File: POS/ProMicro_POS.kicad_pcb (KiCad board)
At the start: 2 copper layers, 17.8 x 30.5 mm, 36 parts, among them J1 uFL, J2 Coax, U1 MPU-9250, U2 AP2112K-1.8, U3 SIM28ML

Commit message: clean
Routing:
- net SDA: track 13.8 -> 14.4 mm
- net GND: vias 49 -> 48

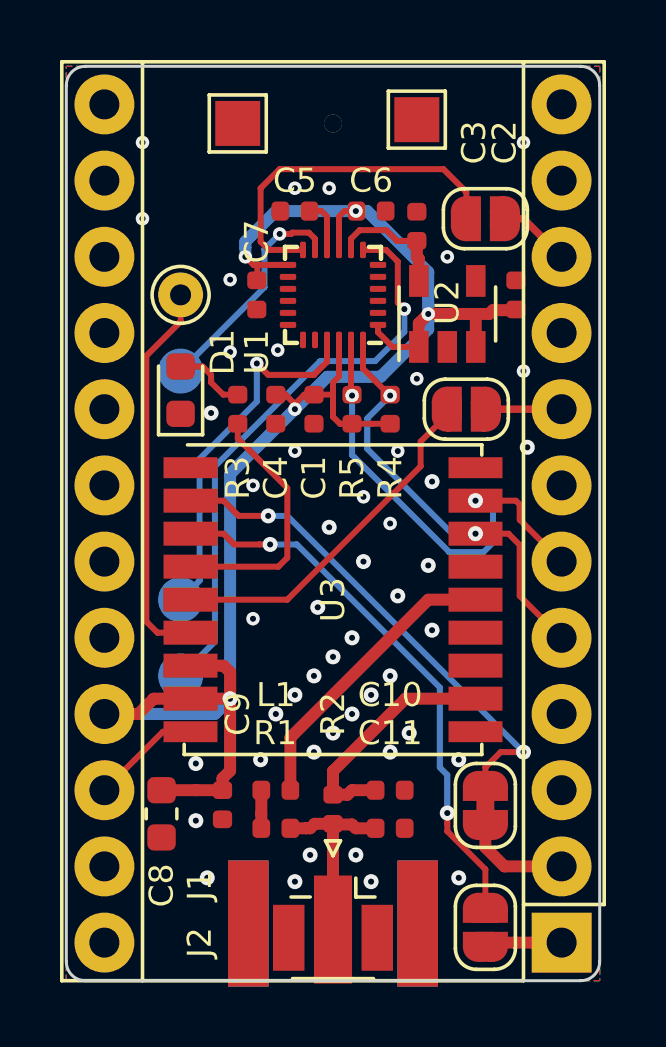
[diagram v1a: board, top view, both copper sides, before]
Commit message: fix ERC/DRC and add power planes
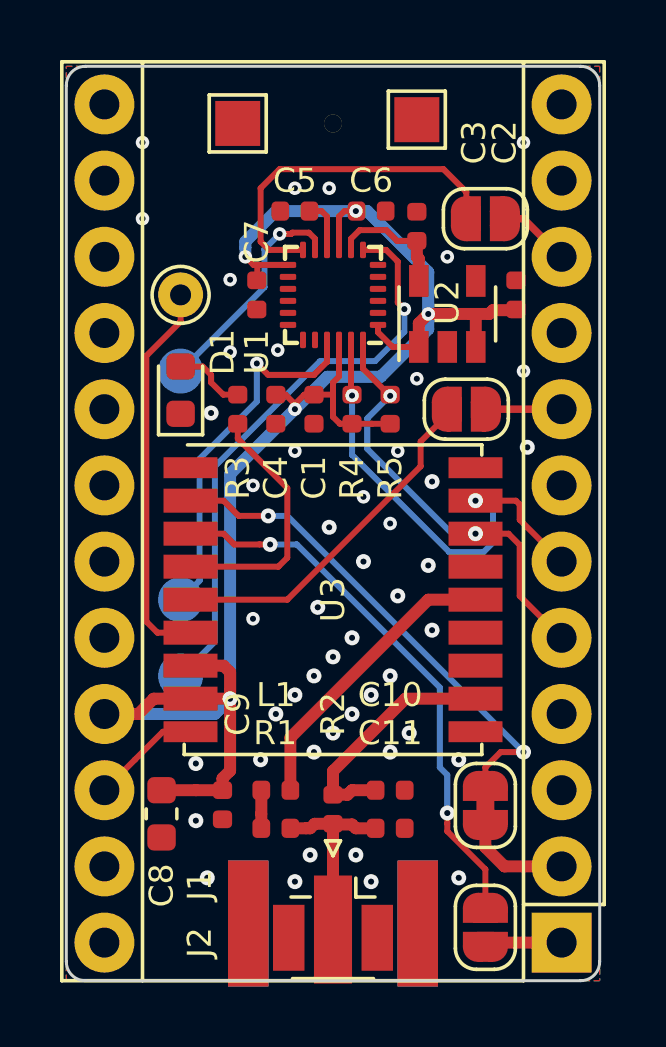
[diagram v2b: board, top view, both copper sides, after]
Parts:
- moved R4 1.27 mm to (145.4, 83.8)
- moved R5 1.27 mm to (146.7, 83.8)
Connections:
- A1 pad 10: (no net) -> INT
- A1 pad 11: (no net) -> Net-(A1-Pad11)
- A1 pad 12: (no net) -> Net-(A1-Pad12)
- A1 pad 13: (no net) -> Net-(A1-Pad13)
- A1 pad 14: (no net) -> Net-(A1-Pad14)
- A1 pad 15: (no net) -> Net-(A1-Pad15)
- A1 pad 16: (no net) -> Net-(A1-Pad16)
- A1 pad 17: (no net) -> Net-(A1-Pad17)
- A1 pad 18: (no net) -> Net-(A1-Pad18)
- A1 pad 19: (no net) -> Net-(A1-Pad19)
- A1 pad 20: (no net) -> Net-(A1-Pad20)
- A1 pad 24: (no net) -> +5V
- A1 pad 7: (no net) -> Net-(A1-Pad7)
- A1 pad 9: (no net) -> Net-(A1-Pad9)
- JP1 pad 2: (no net) -> INT
- R4 pad 2: SDA -> SCL
- R5 pad 2: SCL -> SDA
- U2 pad 4: (no net) -> Net-(U2-Pad4)
- U3 pad 13: (no net) -> Net-(U3-Pad13)
- U3 pad 15: (no net) -> Net-(U3-Pad15)
- U3 pad 18: (no net) -> Net-(U3-Pad18)
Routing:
- net INT: track 0.00 -> 2.43 mm
- net (no net): track 2.43 -> 0.00 mm
- added copper zone on In2.Cu, net +3V3
- added copper zone on In1.Cu, net GND
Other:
- copper layers 2 -> 4
- board text added: "nerdyscout.github.io/ ProMicro/POS v3.3"
- board text removed: "nerdyscout.github.io/ ProMicro/POS v3.1"

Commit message: make controller holes wide enough
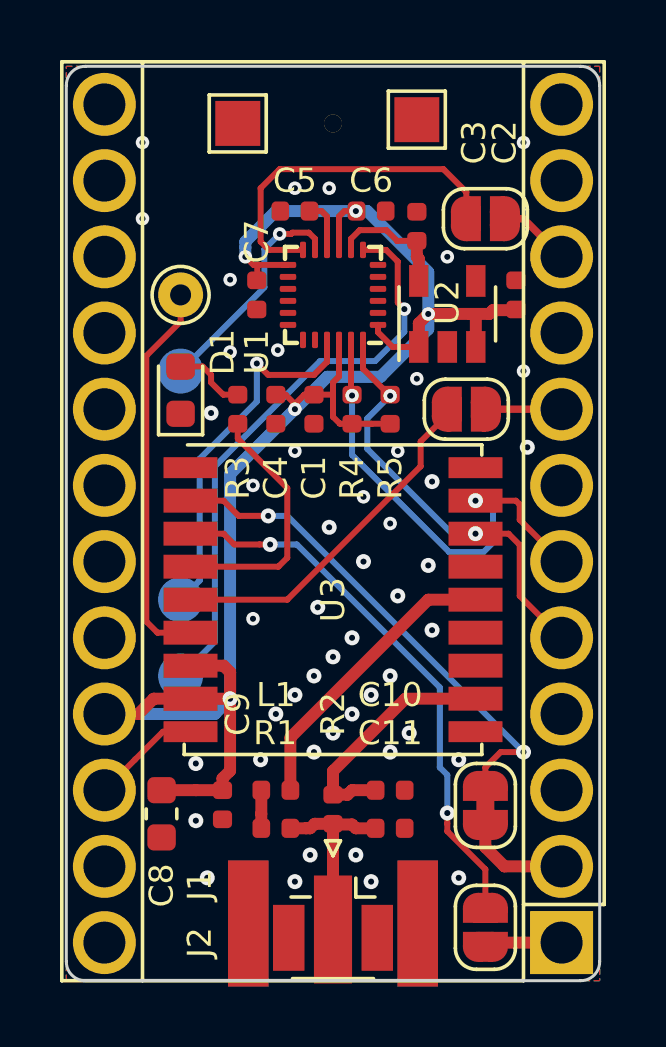
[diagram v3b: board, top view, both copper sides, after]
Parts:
- renumbered A1 to #A1
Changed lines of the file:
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@@
     (mod_text_size 1 1)
     (mod_text_width 0.15)
-    (pad_size 0.6 0.6)
-    (pad_drill 0.6)
+    (pad_size 2.1 2.1)
+    (pad_drill 1.4)
     (pad_to_mask_clearance 0)
     (aux_axis_origin 152.4 101.6)
@@
     (descr "Sparkfun Pro Micro, https://cdn.sparkfun.com/datasheets/Dev/Arduino/Boards/Pro_Micro_v13b.pdf")
     (tags "Sparkfun Pro Micro")
-    (fp_text reference A1 (at 2.54 0 90) (layer F.SilkS) hide
+    (fp_text reference "#A1" (at 2.54 0 90) (layer F.SilkS) hide
       (effects (font (size 0.8 0.8) (thickness 0.2)))
     )
@@
       (effects (font (size 1 1) (thickness 0.15)))
     )
-    (pad 1 thru_hole rect (at 0 0 180) (size 2 2) (drill 1) (layers *.Cu *.Mask)
+    (pad 1 thru_hole rect (at 0 0 180) (size 2.1 2.1) (drill 1.4) (layers *.Cu *.Mask)
       (net 19 RXD))
-    (pad 2 thru_hole oval (at 0 2.54 180) (size 2 2) (drill 1) (layers *.Cu *.Mask)
+    (pad 2 thru_hole circle (at 0 2.54 180) (size 2.1 2.1) (drill 1.4) (layers *.Cu *.Mask)
       (net 20 TXD))
-    (pad 3 thru_hole oval (at 0 5.08 180) (size 2 2) (drill 1) (layers *.Cu *.Mask)
+    (pad 3 thru_hole circle (at 0 5.08 180) (size 2.1 2.1) (drill 1.4) (layers *.Cu *.Mask)
       (net 1 GND))
-    (pad 13 thru_hole oval (at 15.24 27.94 180) (size 2 2) (drill 1) (layers *.Cu *.Mask)
+    (pad 13 thru_hole circle (at 15.24 27.94 180) (size 2.1 2.1) (drill 1.4) (layers *.Cu *.Mask)
       (net 25 "Net-(A1-Pad13)"))
-    (pad 4 thru_hole oval (at 0 7.62 180) (size 2 2) (drill 1) (layers *.Cu *.Mask)
+    (pad 4 thru_hole circle (at 0 7.62 180) (size 2.1 2.1) (drill 1.4) (layers *.Cu *.Mask)
       (net 1 GND))
-    (pad 14 thru_hole oval (at 15.24 25.4 180) (size 2 2) (drill 1) (layers *.Cu *.Mask)
+    (pad 14 thru_hole circle (at 15.24 25.4 180) (size 2.1 2.1) (drill 1.4) (layers *.Cu *.Mask)
       (net 26 "Net-(A1-Pad14)"))
-    (pad 5 thru_hole oval (at 0 10.16 180) (size 2 2) (drill 1) (layers *.Cu *.Mask)
+    (pad 5 thru_hole circle (at 0 10.16 180) (size 2.1 2.1) (drill 1.4) (layers *.Cu *.Mask)
       (net 21 SDA))
-    (pad 15 thru_hole oval (at 15.24 22.86 180) (size 2 2) (drill 1) (layers *.Cu *.Mask)
+    (pad 15 thru_hole circle (at 15.24 22.86 180) (size 2.1 2.1) (drill 1.4) (layers *.Cu *.Mask)
       (net 27 "Net-(A1-Pad15)"))
-    (pad 6 thru_hole oval (at 0 12.7 180) (size 2 2) (drill 1) (layers *.Cu *.Mask)
+    (pad 6 thru_hole circle (at 0 12.7 180) (size 2.1 2.1) (drill 1.4) (layers *.Cu *.Mask)
       (net 22 SCL))
-    (pad 16 thru_hole oval (at 15.24 20.32 180) (size 2 2) (drill 1) (layers *.Cu *.Mask)
+    (pad 16 thru_hole circle (at 15.24 20.32 180) (size 2.1 2.1) (drill 1.4) (layers *.Cu *.Mask)
       (net 28 "Net-(A1-Pad16)"))
-    (pad 7 thru_hole oval (at 0 15.24 180) (size 2 2) (drill 1) (layers *.Cu *.Mask)
+    (pad 7 thru_hole circle (at 0 15.24 180) (size 2.1 2.1) (drill 1.4) (layers *.Cu *.Mask)
       (net 29 "Net-(A1-Pad7)"))
-    (pad 17 thru_hole oval (at 15.24 17.78 180) (size 2 2) (drill 1) (layers *.Cu *.Mask)
+    (pad 17 thru_hole circle (at 15.24 17.78 180) (size 2.1 2.1) (drill 1.4) (layers *.Cu *.Mask)
       (net 30 "Net-(A1-Pad17)"))
-    (pad 8 thru_hole oval (at 0 17.78 180) (size 2 2) (drill 1) (layers *.Cu *.Mask)
+    (pad 8 thru_hole circle (at 0 17.78 180) (size 2.1 2.1) (drill 1.4) (layers *.Cu *.Mask)
       (net 23 PWM))
-    (pad 18 thru_hole oval (at 15.24 15.24 180) (size 2 2) (drill 1) (layers *.Cu *.Mask)
+    (pad 18 thru_hole circle (at 15.24 15.24 180) (size 2.1 2.1) (drill 1.4) (layers *.Cu *.Mask)
       (net 31 "Net-(A1-Pad18)"))
-    (pad 9 thru_hole oval (at 0 20.32 180) (size 2 2) (drill 1) (layers *.Cu *.Mask)
+    (pad 9 thru_hole circle (at 0 20.32 180) (size 2.1 2.1) (drill 1.4) (layers *.Cu *.Mask)
       (net 32 "Net-(A1-Pad9)"))
-    (pad 19 thru_hole oval (at 15.24 12.7 180) (size 2 2) (drill 1) (layers *.Cu *.Mask)
+    (pad 19 thru_hole circle (at 15.24 12.7 180) (size 2.1 2.1) (drill 1.4) (layers *.Cu *.Mask)
       (net 33 "Net-(A1-Pad19)"))
-    (pad 10 thru_hole oval (at 0 22.86 180) (size 2 2) (drill 1) (layers *.Cu *.Mask)
+    (pad 10 thru_hole circle (at 0 22.86 180) (size 2.1 2.1) (drill 1.4) (layers *.Cu *.Mask)
       (net 34 INT))
-    (pad 20 thru_hole oval (at 15.24 10.16 180) (size 2 2) (drill 1) (layers *.Cu *.Mask)
+    (pad 20 thru_hole circle (at 15.24 10.16 180) (size 2.1 2.1) (drill 1.4) (layers *.Cu *.Mask)
       (net 35 "Net-(A1-Pad20)"))
-    (pad 11 thru_hole oval (at 0 25.4 180) (size 2 2) (drill 1) (layers *.Cu *.Mask)
+    (pad 11 thru_hole circle (at 0 25.4 180) (size 2.1 2.1) (drill 1.4) (layers *.Cu *.Mask)
       (net 36 "Net-(A1-Pad11)"))
-    (pad 21 thru_hole oval (at 15.24 7.62 180) (size 2 2) (drill 1) (layers *.Cu *.Mask)
+    (pad 21 thru_hole circle (at 15.24 7.62 180) (size 2.1 2.1) (drill 1.4) (layers *.Cu *.Mask)
       (net 2 +3V3))
-    (pad 12 thru_hole oval (at 0 27.94 180) (size 2 2) (drill 1) (layers *.Cu *.Mask)
+    (pad 12 thru_hole circle (at 0 27.94 180) (size 2.1 2.1) (drill 1.4) (layers *.Cu *.Mask)
       (net 37 "Net-(A1-Pad12)"))
-    (pad 22 thru_hole oval (at 15.24 5.08 180) (size 2 2) (drill 1) (layers *.Cu *.Mask)
+    (pad 22 thru_hole circle (at 15.24 5.08 180) (size 2.1 2.1) (drill 1.4) (layers *.Cu *.Mask)
       (net 24 ~RST))
-    (pad 23 thru_hole oval (at 15.24 2.54 180) (size 2 2) (drill 1) (layers *.Cu *.Mask)
+    (pad 23 thru_hole circle (at 15.24 2.54 180) (size 2.1 2.1) (drill 1.4) (layers *.Cu *.Mask)
       (net 1 GND))
-    (pad 24 thru_hole oval (at 15.24 0 180) (size 2 2) (drill 1) (layers *.Cu *.Mask)
+    (pad 24 thru_hole circle (at 15.24 0 180) (size 2.1 2.1) (drill 1.4) (layers *.Cu *.Mask)
       (net 38 +5V))
     (model ${KISYS3DMOD}/Module.3dshapes/Sparkfun_Pro_Micro.wrl

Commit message: update PCBS
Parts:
- renumbered #A1 to A1
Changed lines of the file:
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@@
     (descr "Sparkfun Pro Micro, https://cdn.sparkfun.com/datasheets/Dev/Arduino/Boards/Pro_Micro_v13b.pdf")
     (tags "Sparkfun Pro Micro")
-    (fp_text reference "#A1" (at 2.54 0 90) (layer F.SilkS) hide
+    (fp_text reference A1 (at 2.54 0 90) (layer F.SilkS) hide
       (effects (font (size 0.8 0.8) (thickness 0.2)))
     )
